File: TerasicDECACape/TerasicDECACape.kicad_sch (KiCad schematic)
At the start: 38 parts, among them CN1 NASB0-S6701-TS50, CN2 NASB0-S6701-TS50, J1 MiSTer SDRAM Module, J2 USB_A, J3 Conn_01x03_Male, J4 Conn_02x06_Odd_Even, P8 BeagleBone_Black_Header, P9 BeagleBone_Black_Header, SW1 TS-1187A-B-A-B, SW2 TS-1187A-B-A-B

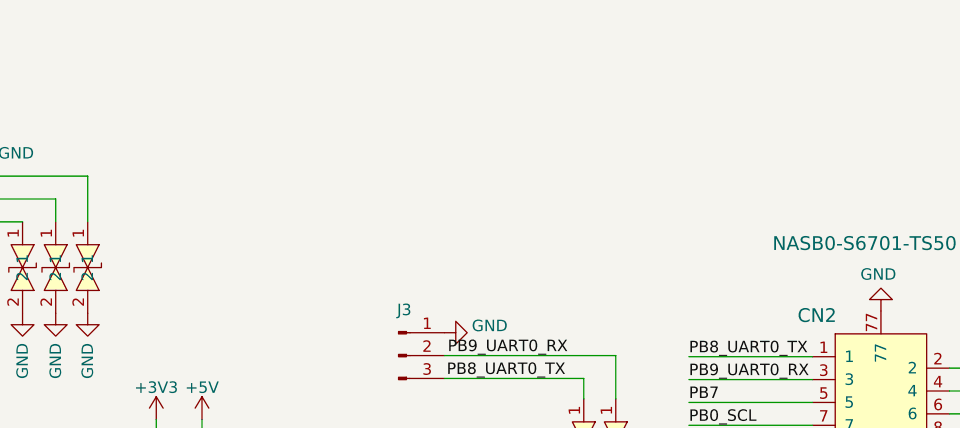
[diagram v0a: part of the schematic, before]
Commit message: add ground headers, ground test points and ground vias
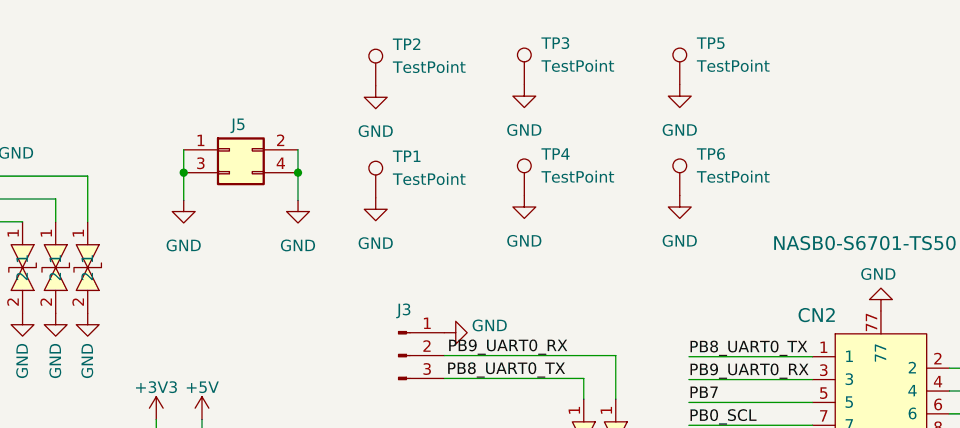
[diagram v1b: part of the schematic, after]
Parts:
- added J5: Conn_02x02_Odd_Even, Connector_PinHeader_2.54mm:PinHeader_2x02_P2.54mm_Vertical, symbol Connector_Generic:Conn_02x02_Odd_Even
- added TP1, TP4: TestPoint, TestPoint:TestPoint_Pad_D2.0mm, symbol Connector:TestPoint
- added TP2, TP3, TP5, TP6: TestPoint, TestPoint:TestPoint_Pad_D1.0mm, symbol Connector:TestPoint
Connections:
- net GND: now also J5.1 (Pin_1), J5.2 (Pin_2), J5.3 (Pin_3), J5.4 (Pin_4), TP1.1, TP2.1, TP3.1, TP4.1, TP5.1, TP6.1
